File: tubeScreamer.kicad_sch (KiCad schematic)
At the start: 51 parts, among them J1 IN, J2 IN, J3 OUT, J4 9V IN, J5 OUT, Q1 MMBT2222A, Q2 MMBT2222A, U1 TL072, U2 TL072

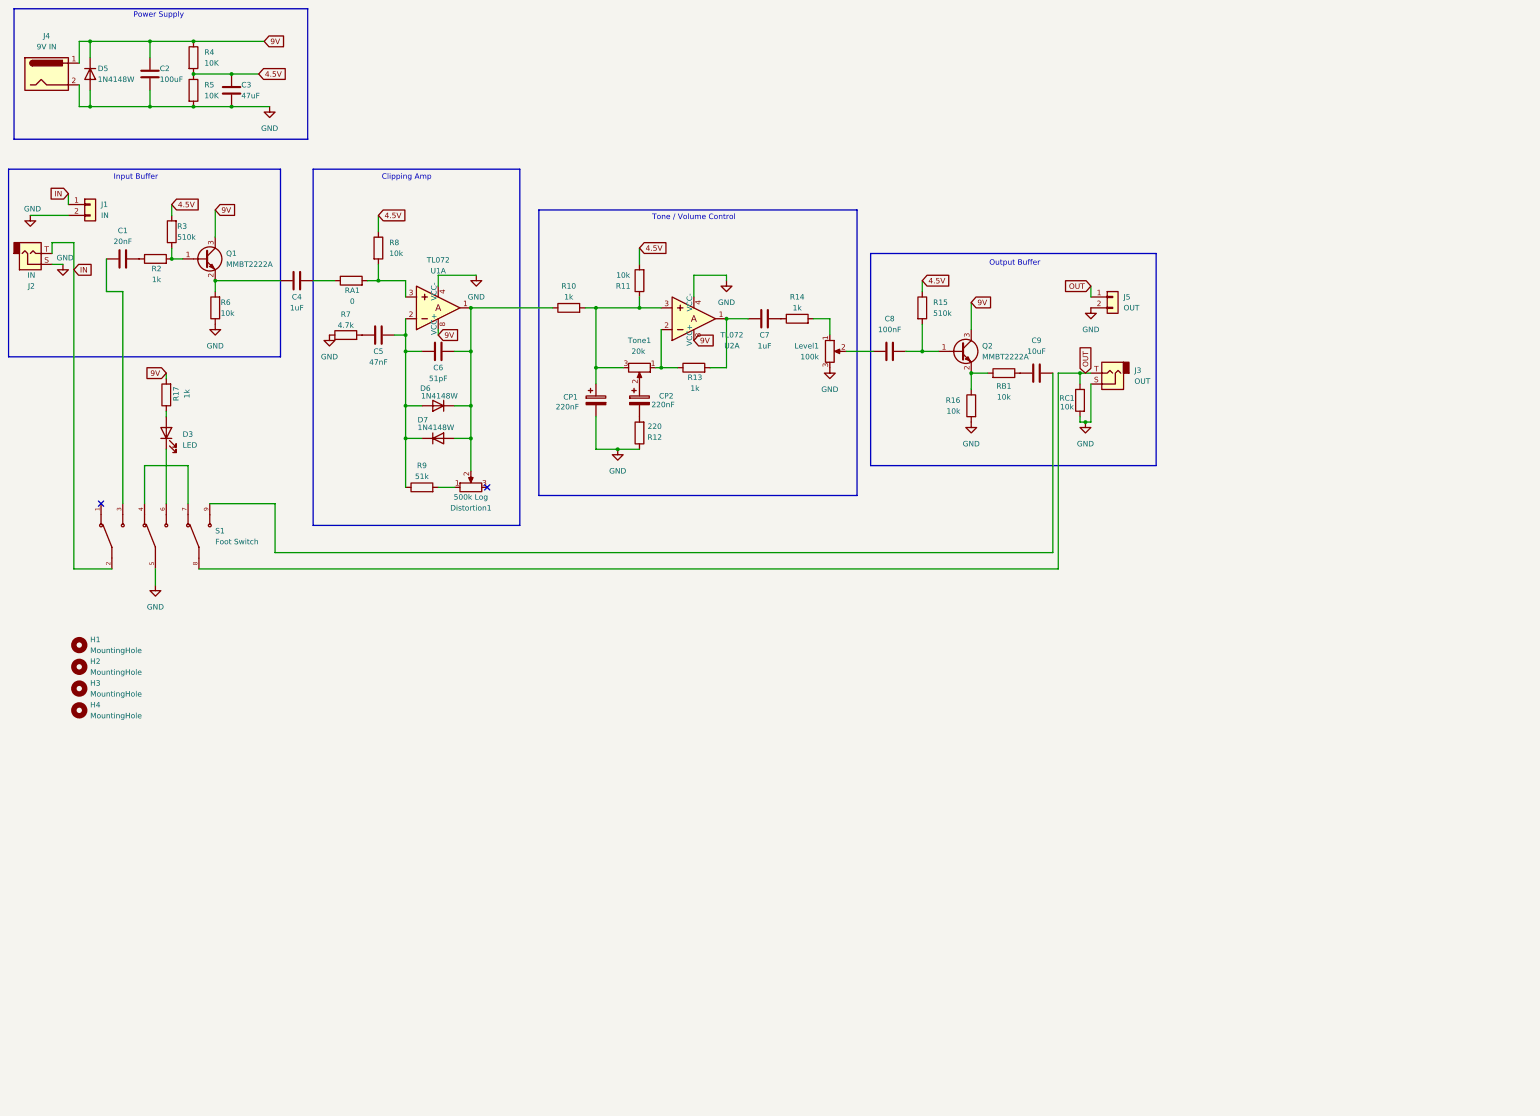
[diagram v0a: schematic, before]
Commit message: updated schematic and PCB layout, 70 x 100 size, updated footprints of footswitch, Barrel Conn, audio jacks, LED and Pots, 9v Battery Compatable, corrected pot polarity, Power is cut at switch, No more 0 ohm Resister.
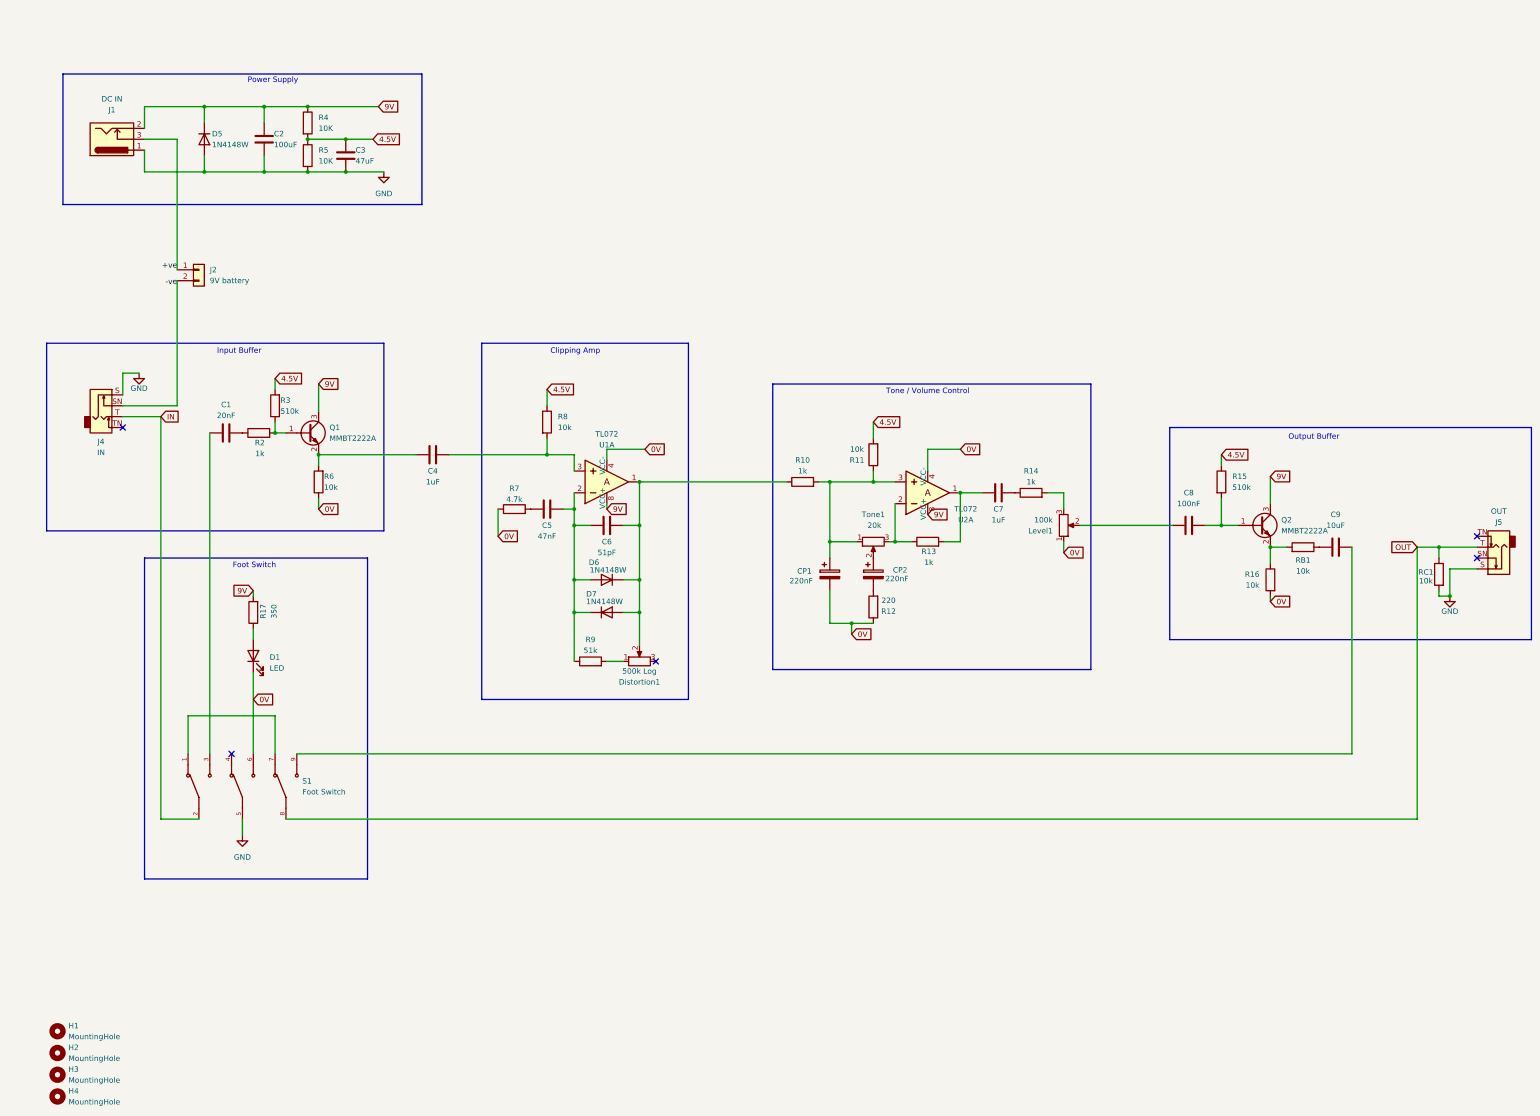
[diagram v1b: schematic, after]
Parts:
- removed D3: LED, LED_SMD:LED_0603_1608Metric, symbol Device:LED
- removed J1: IN, Connector_Wire:SolderWire-0.25sqmm_1x02_P4.2mm_D0.65mm_OD1.7mm, symbol Connector_Generic:Conn_01x02
- removed J2: IN, Connector_Audio:Jack_6.35mm_Neutrik_NMJ4HFD2_Horizontal, symbol Connector_Audio:AudioJack2
- removed J3: OUT, Connector_Audio:Jack_6.35mm_Neutrik_NMJ4HFD2_Horizontal, symbol Connector_Audio:NJ2FD-V
- removed J4: 9V IN, Connector_BarrelJack:BarrelJack_CUI_PJ-063AH_Horizontal, symbol Connector:Barrel_Jack
- removed J5: OUT, Connector_Wire:SolderWire-0.25sqmm_1x02_P4.2mm_D0.65mm_OD1.7mm, symbol Connector_Generic:Conn_01x02
- removed RA1: 0, Jumper:SolderJumper-2_P1.3mm_Open_Pad1.0x1.5mm, symbol Device:R
- added D1: LED, LED_THT:LED_D3.0mm_Clear, symbol Device:LED
- added J1: DC IN, Connector_BarrelJack:BarrelJack_GCT_DCJ200-10-A_Horizontal, symbol Connector:Barrel_Jack_Switch
- added J2: 9V battery, Connector_PinSocket_2.00mm:PinSocket_1x02_P2.00mm_Vertical, symbol Connector_Generic:Conn_01x02
- added J4: IN, Connector_Audio:Jack_6.35mm_Neutrik_NMJ6HFD2_Horizontal, symbol Connector_Audio:AudioJack2_Switch
- added J5: OUT, Connector_Audio:Jack_6.35mm_Neutrik_NMJ6HFD2_Horizontal, symbol Connector_Audio:AudioJack2_Switch
- Distortion1: footprint Rotary_Encoder:RotaryEncoder_Bourns_Vertical_PEC12R-3x17F-Nxxxx -> Potentiometer_THT:Potentiometer_RK097_Single_Vertical
- Level1, Tone1: footprint digikey-footprints:Potentiometer_P120PK-Y25BR10K -> Potentiometer_THT:Potentiometer_RK097_Single_Vertical
- R17: value 1k -> 350
- S1: footprint FS57003PLT2B2M2QE:SW_FS57003PLT2B2M2QE -> Button_Switch_THT:3PDT Foot Switch; MANUFACTURER E-Switch -> (none); MAXIMUM_PACKAGE_HEIGHT 38.2mm -> (none); PARTREV 4.2.2018 -> (none); SNAPEDA_PN FS57003PLT2B2M2QE -> (none); STANDARD Manufacturer Recommendations -> (none)
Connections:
- net 9V: now also J1.2
- net GND: now also J1.1, J4.S, J5.S; no longer CP1.2, Level1.3, R12.1, R16.2, R6.1, R7.1, U1.4 (VCC-), U2.4 (VCC-)
- net IN: now also J4.T
- net OUT: now also J5.T
- net at CP1.1, R10.2, R11.1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: now also Tone1.1; no longer Tone1.3
- net at R8.2, U1.3: now also C4.2
- net at R13.1, U2.2: now also Tone1.3; no longer Tone1.1
- net at R14.2: now also Level1.3; no longer Level1.1
- net at R17.1: now also D1.2 (A)
- net at S1.1: now also S1.7
- net at S1.4: no longer S1.7
- net 0V: now reaches S1.6
- net 0V: now also CP1.2, Level1.1, R12.1, R16.2, R6.1, R7.1, U1.4 (VCC-), U2.4 (VCC-), D1.1 (K)
- new net +ve: J1.3, J2.1 (Pin_1)
- new net -ve: J2.2 (Pin_2), J4.SN
- no-connect marks 2 -> 5
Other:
- note added: "Foot Switch"
- moved on the sheet: C1, C2, C3, C4, C5, C6, C7, C8, C9, CP1, CP2, D5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
